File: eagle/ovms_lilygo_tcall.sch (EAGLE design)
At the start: 45 parts, among them IC2 SN65HVD233, IC3 SN65HVD233, IC4 LMR516XX, IC5 MCP2515, Q1 X49SM16MSD2SC

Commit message: Correct width an hole position of case
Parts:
- R11: value 47k -> 470k
- R3: value 22k -> 220k
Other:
- note added: "LMR51610 EN thresholds ON: 1.22V OFF 1.0V Choice of R3 Von Voff 180k 11.7V 11.4V 220k 11.8V 11.4V 270k 11.9V 11.5V 300k 12.0V 11.6V Values depend on the actual Zener voltage (nominal 10V) at low current (2.8µA)."
- note removed: "EN threshold 11.5V DISABLE threshold 9V"
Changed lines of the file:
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@@
 <part name="SEL12V" library="jumper" library_urn="urn:adsk.eagle:library:252" deviceset="SJ2W" device="" package3d_urn="urn:adsk.eagle:package:15474/1"/>
 <part name="IC4" library="ovms_lilygo" deviceset="LMR516XX" device="" package3d_urn="urn:adsk.eagle:package:30993/1"/>
-<part name="R3" library="rcl" library_urn="urn:adsk.eagle:library:334" deviceset="R-EU_" device="M0805" package3d_urn="urn:adsk.eagle:package:23556/2" value="22k"/>
+<part name="R3" library="rcl" library_urn="urn:adsk.eagle:library:334" deviceset="R-EU_" device="M0805" package3d_urn="urn:adsk.eagle:package:23556/2" value="220k"/>
 <part name="L2" library="inductors" library_urn="urn:adsk.eagle:library:243" deviceset="DR74" device="" package3d_urn="urn:adsk.eagle:package:15122/1" value="33u"/>
 <part name="C4" library="rcl" library_urn="urn:adsk.eagle:library:334" deviceset="C-EU" device="C0805K" package3d_urn="urn:adsk.eagle:package:23681/2" value="100n"/>
@@
 <part name="R9" library="rcl" library_urn="urn:adsk.eagle:library:334" deviceset="R-EU_" device="M0805" package3d_urn="urn:adsk.eagle:package:23556/2" value="20k"/>
 <part name="GND12" library="supply1" deviceset="GND" device=""/>
-<part name="R11" library="rcl" library_urn="urn:adsk.eagle:library:334" deviceset="R-EU_" device="M0805" package3d_urn="urn:adsk.eagle:package:23556/2" value="47k"/>
+<part name="R11" library="rcl" library_urn="urn:adsk.eagle:library:334" deviceset="R-EU_" device="M0805" package3d_urn="urn:adsk.eagle:package:23556/2" value="470k"/>
 <part name="GND6" library="supply1" deviceset="GND" device=""/>
 <part name="C16" library="rcl" library_urn="urn:adsk.eagle:library:334" deviceset="C-EU" device="C0805K" package3d_urn="urn:adsk.eagle:package:23681/2" value="1u"/>
@@
 P9 - +12V
  </text>
-<text x="-180.34" y="-15.24" size="1.778" layer="97">EN threshold         11.5V
-DISABLE threshold  9V</text>
+<text x="-119.38" y="-38.1" size="1.778" layer="97">LMR51610 EN thresholds
+ON: 1.22V OFF 1.0V
+Choice of R3
+             Von        Voff
+180k       11.7V     11.4V
+220k       11.8V     11.4V
+270k       11.9V     11.5V
+300k       12.0V     11.6V
+Values depend on the actual
+Zener voltage (nominal 10V) at
+low current (2.8µA). </text>
 </plain>
 <instances>

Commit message: Clean up Eagle
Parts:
- C12: device rcl:C-EUC3216 -> rcl:C-EUC1206K
- R1: value 47k -> 470k
- R2: value 10k -> 100k
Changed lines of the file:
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@@
 <attribute name="VIN" value="12V"/>
 </part>
-<part name="R1" library="rcl" library_urn="urn:adsk.eagle:library:334" deviceset="R-EU_" device="M0805" package3d_urn="urn:adsk.eagle:package:23556/2" value="47k"/>
-<part name="R2" library="rcl" library_urn="urn:adsk.eagle:library:334" deviceset="R-EU_" device="M0805" package3d_urn="urn:adsk.eagle:package:23556/2" value="10k"/>
+<part name="R1" library="rcl" library_urn="urn:adsk.eagle:library:334" deviceset="R-EU_" device="M0805" package3d_urn="urn:adsk.eagle:package:23556/2" value="470k"/>
+<part name="R2" library="rcl" library_urn="urn:adsk.eagle:library:334" deviceset="R-EU_" device="M0805" package3d_urn="urn:adsk.eagle:package:23556/2" value="100k"/>
 <part name="C1" library="rcl" library_urn="urn:adsk.eagle:library:334" deviceset="C-EU" device="C0805K" package3d_urn="urn:adsk.eagle:package:23681/2" value="100n"/>
 <part name="C2" library="rcl" library_urn="urn:adsk.eagle:library:334" deviceset="C-EU" device="C0805K" package3d_urn="urn:adsk.eagle:package:23681/2" value="1u"/>
@@
 <part name="C8" library="rcl" library_urn="urn:adsk.eagle:library:334" deviceset="C-EU" device="C0805K" package3d_urn="urn:adsk.eagle:package:23681/2" value="1u"/>
 <part name="C9" library="rcl" library_urn="urn:adsk.eagle:library:334" deviceset="C-EU" device="C0805K" package3d_urn="urn:adsk.eagle:package:23681/2" value="1u"/>
-<part name="C12" library="rcl" library_urn="urn:adsk.eagle:library:334" deviceset="C-EU" device="C3216" package3d_urn="urn:adsk.eagle:package:23628/2" value="22u"/>
+<part name="C12" library="rcl" library_urn="urn:adsk.eagle:library:334" deviceset="C-EU" device="C1206K" package3d_urn="urn:adsk.eagle:package:23682/2" value="22u"/>
 <part name="C14" library="rcl" library_urn="urn:adsk.eagle:library:334" deviceset="C-EU" device="C1206K" package3d_urn="urn:adsk.eagle:package:23682/2" value="22u"/>
 <part name="C15" library="rcl" library_urn="urn:adsk.eagle:library:334" deviceset="C-EU" device="C0805K" package3d_urn="urn:adsk.eagle:package:23681/2" value="2u2"/>
@@
 </instance>
 <instance part="C14" gate="G$1" x="-147.32" y="7.62" smashed="yes" rot="R180">
-<attribute name="NAME" x="-148.844" y="7.239" size="1.778" layer="95" rot="R180"/>
+<attribute name="NAME" x="-148.844" y="9.779" size="1.778" layer="95" rot="R180"/>
 <attribute name="VALUE" x="-148.844" y="12.319" size="1.778" layer="96" rot="R180"/>
 </instance>

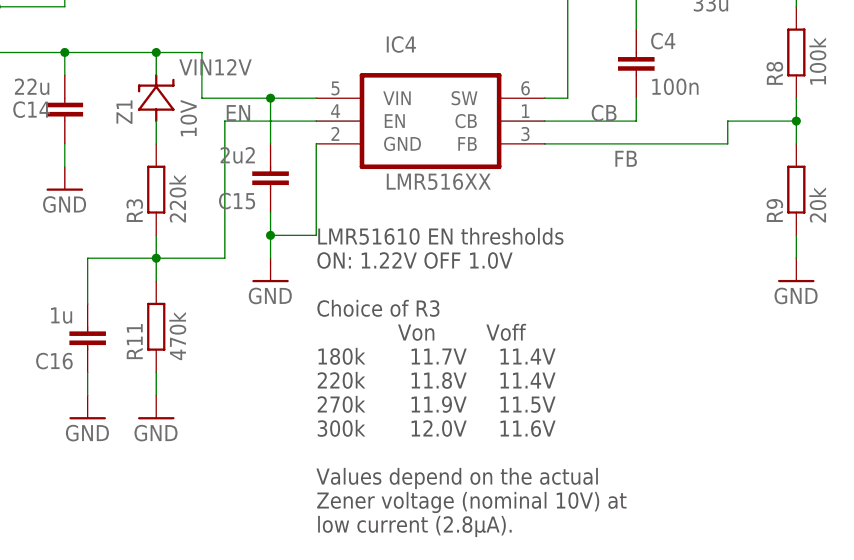
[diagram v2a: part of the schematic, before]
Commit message: Adjust resistors for low current (DCDC off)
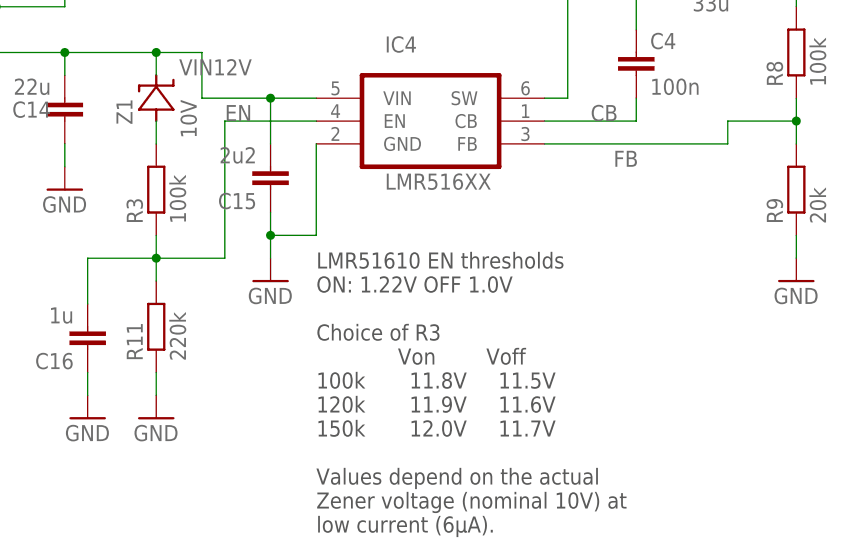
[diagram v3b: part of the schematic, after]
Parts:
- R11: value 470k -> 220k
- R3: value 220k -> 100k
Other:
- note added: "LMR51610 EN thresholds ON: 1.22V OFF 1.0V Choice of R3 Von Voff 100k 11.8V 11.5V 120k 11.9V 11.6V 150k 12.0V 11.7V Values depend on the actual Zener voltage (nominal 10V) at low current (6µA)."
- note removed: "LMR51610 EN thresholds ON: 1.22V OFF 1.0V Choice of R3 Von Voff 180k 11.7V 11.4V 220k 11.8V 11.4V 270k 11.9V 11.5V 300k 12.0V 11.6V Values depend on the actual Zener voltage (nominal 10V) at low current (2.8µA)."
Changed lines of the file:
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@@
 <part name="SEL12V" library="jumper" library_urn="urn:adsk.eagle:library:252" deviceset="SJ2W" device="" package3d_urn="urn:adsk.eagle:package:15474/1"/>
 <part name="IC4" library="ovms_lilygo" deviceset="LMR516XX" device="" package3d_urn="urn:adsk.eagle:package:30993/1"/>
-<part name="R3" library="rcl" library_urn="urn:adsk.eagle:library:334" deviceset="R-EU_" device="M0805" package3d_urn="urn:adsk.eagle:package:23556/2" value="220k"/>
+<part name="R3" library="rcl" library_urn="urn:adsk.eagle:library:334" deviceset="R-EU_" device="M0805" package3d_urn="urn:adsk.eagle:package:23556/2" value="100k"/>
 <part name="L2" library="inductors" library_urn="urn:adsk.eagle:library:243" deviceset="DR74" device="" package3d_urn="urn:adsk.eagle:package:15122/1" value="33u"/>
 <part name="C4" library="rcl" library_urn="urn:adsk.eagle:library:334" deviceset="C-EU" device="C0805K" package3d_urn="urn:adsk.eagle:package:23681/2" value="100n"/>
@@
 <part name="R9" library="rcl" library_urn="urn:adsk.eagle:library:334" deviceset="R-EU_" device="M0805" package3d_urn="urn:adsk.eagle:package:23556/2" value="20k"/>
 <part name="GND12" library="supply1" deviceset="GND" device=""/>
-<part name="R11" library="rcl" library_urn="urn:adsk.eagle:library:334" deviceset="R-EU_" device="M0805" package3d_urn="urn:adsk.eagle:package:23556/2" value="470k"/>
+<part name="R11" library="rcl" library_urn="urn:adsk.eagle:library:334" deviceset="R-EU_" device="M0805" package3d_urn="urn:adsk.eagle:package:23556/2" value="220k"/>
 <part name="GND6" library="supply1" deviceset="GND" device=""/>
 <part name="C16" library="rcl" library_urn="urn:adsk.eagle:library:334" deviceset="C-EU" device="C0805K" package3d_urn="urn:adsk.eagle:package:23681/2" value="1u"/>
@@
 Choice of R3
              Von        Voff
-180k       11.7V     11.4V
-220k       11.8V     11.4V
-270k       11.9V     11.5V
-300k       12.0V     11.6V
+100k       11.8V     11.5V
+120k       11.9V     11.6V
+150k       12.0V     11.7V
 Values depend on the actual
 Zener voltage (nominal 10V) at
-low current (2.8µA). </text>
+low current (6µA). </text>
 </plain>
 <instances>
